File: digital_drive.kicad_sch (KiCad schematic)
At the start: 0 parts

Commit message: a bunch of updates
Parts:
- added U1601, U1602: EPC23104ENGRT, BR_Gate_Drivers:EPC23104, symbol BR_PMIC:EPC23104ENGRT

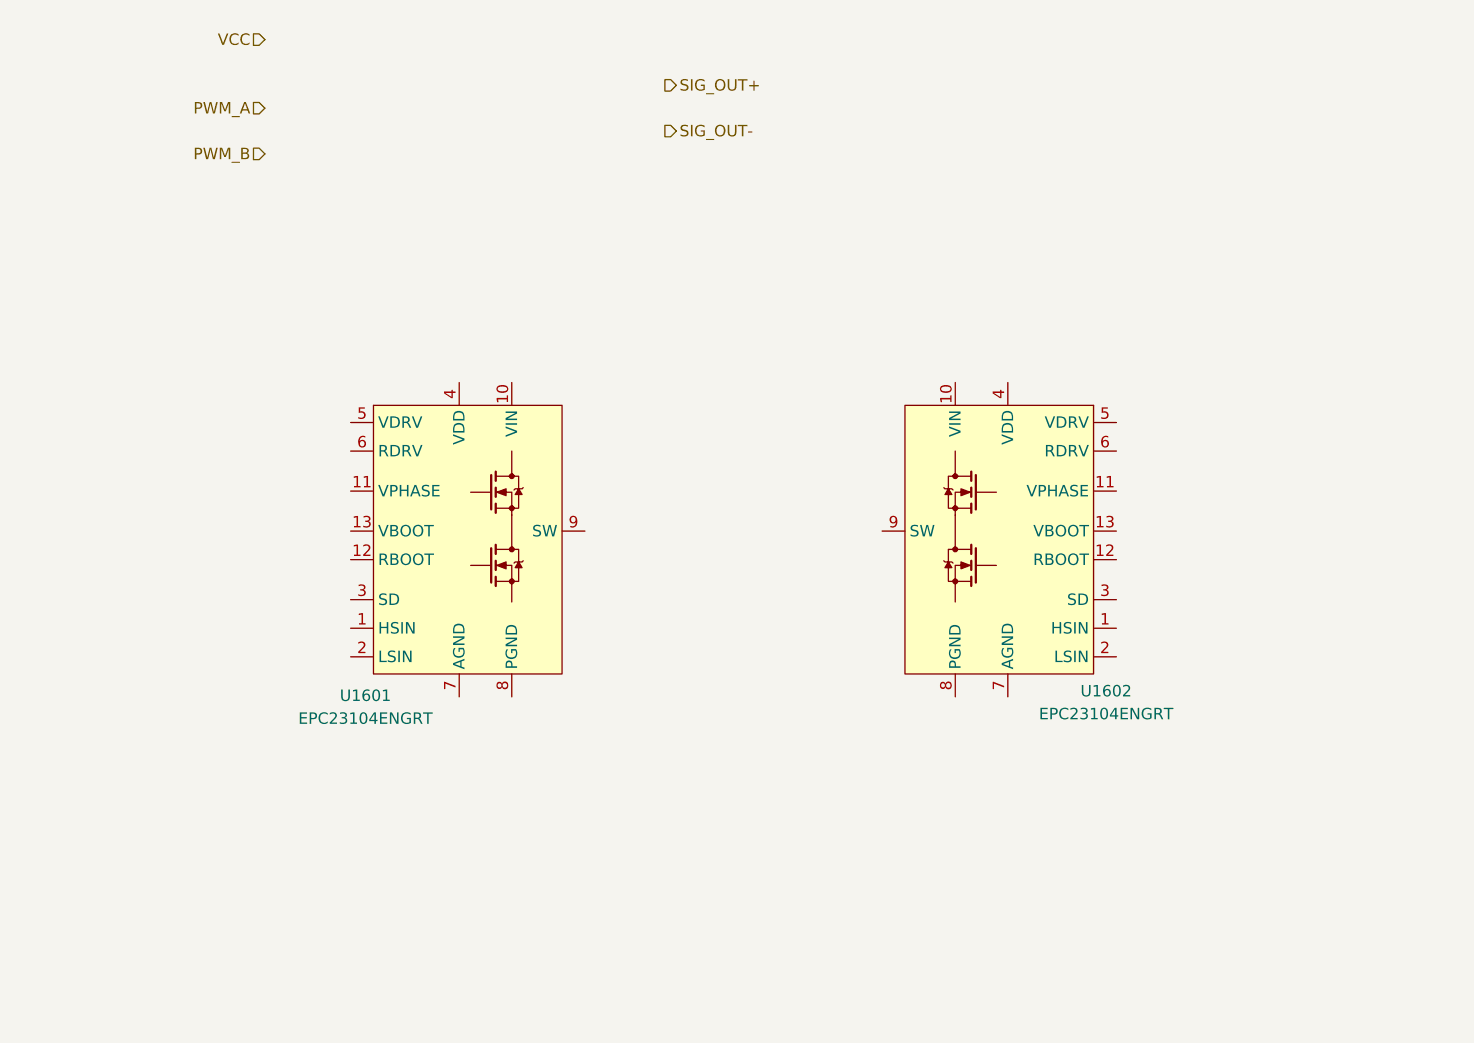
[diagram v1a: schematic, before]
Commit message: added rj45 and h-bridge + stm pinout spreadsheet
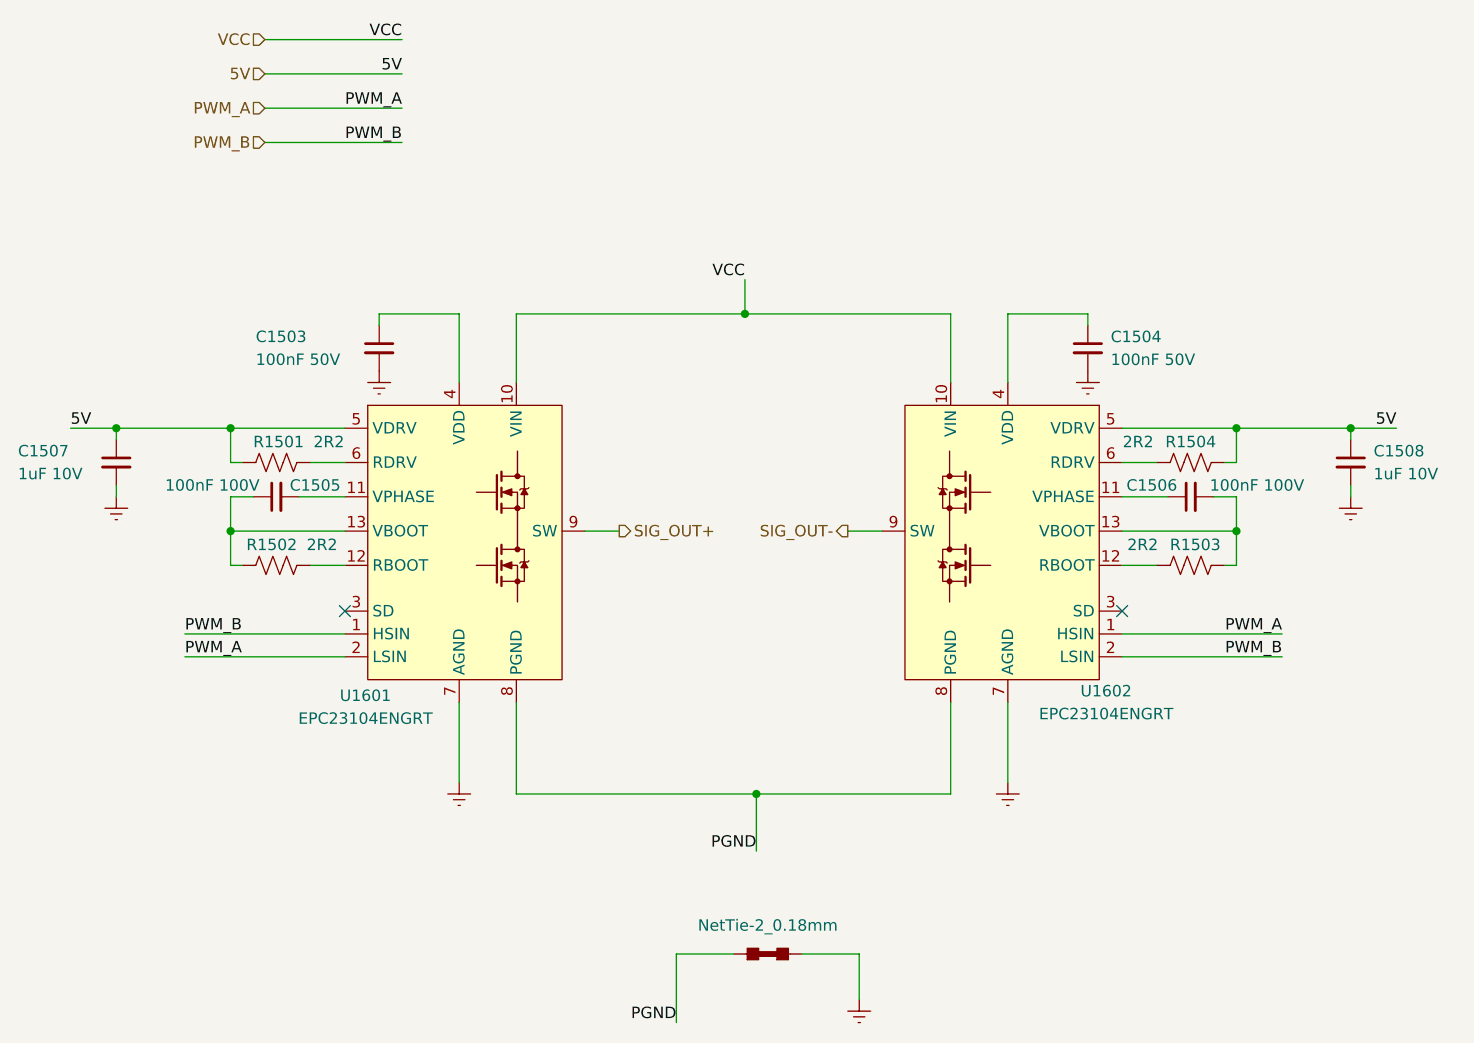
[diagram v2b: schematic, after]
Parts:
- added C1503, C1504: 100nF 50V, BR_Passives:C_0402_1005Metric-minimized, symbol BR_Capacitors_0402:C_0402_100nF_50V_X7R_10%_AEC-Q200
- added C1505, C1506: 100nF 100V, BR_Passives:C_0603_1608Metric-minimized, symbol BR_Capacitors_0603:C_0603_100nF_100V_X7R_AEC-Q200
- added C1507, C1508: 1uF 10V, BR_Passives:C_0402_1005Metric-minimized, symbol BR_Capacitors_0402:C_0402_1uF_10V_X7R_10%
- added NT1501: NetTie-2_0.18mm, BR_Virtual_Parts:NetTie-2_SMD_Pad_0.18mm_wide_long, symbol BR_Virtual_Parts:NetTie-2_0.18mm_long
- added R1501, R1502, R1503, R1504: 2R2, BR_Passives:R_0402_1005Metric-minimized, symbol BR_Resistors_0402:R_0402_2R2
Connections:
- net PWM_A: now also U1601.2 (LSIN), U1602.1 (HSIN)
- net PWM_B: now also U1601.1 (HSIN), U1602.2 (LSIN)
- net SIG_OUT+: now also U1601.9 (SW)
- net SIG_OUT-: now also U1602.9 (SW)
- net VCC: now also U1601.10 (VIN), U1602.10 (VIN)
- net at U1601.11 (VPHASE): now also C1505.2
- net at U1601.12 (RBOOT): now also R1502.2
- net at U1601.13 (VBOOT): now also C1505.1, R1502.1
- net at U1601.4 (VDD): now also C1503.1
- net 5V: now reaches U1601.5 (VDRV)
- net 5V: now also U1602.5 (VDRV), C1507.1, C1508.1, R1501.1, R1504.2
- net at U1601.6 (RDRV): now also R1501.2
- net GND: now reaches U1601.7 (AGND)
- net GND: now also U1602.7 (AGND), C1503.2, C1504.2, C1507.2, C1508.2, NT1501.2
- net PGND: now reaches U1601.8 (PGND)
- net PGND: now also U1602.8 (PGND), NT1501.1
- net at U1602.11 (VPHASE): now also C1506.1
- net at U1602.12 (RBOOT): now also R1503.1
- net at U1602.13 (VBOOT): now also C1506.2, R1503.2
- net at U1602.4 (VDD): now also C1504.1
- net at U1602.6 (RDRV): now also R1504.1
- no-connect marks 0 -> 2

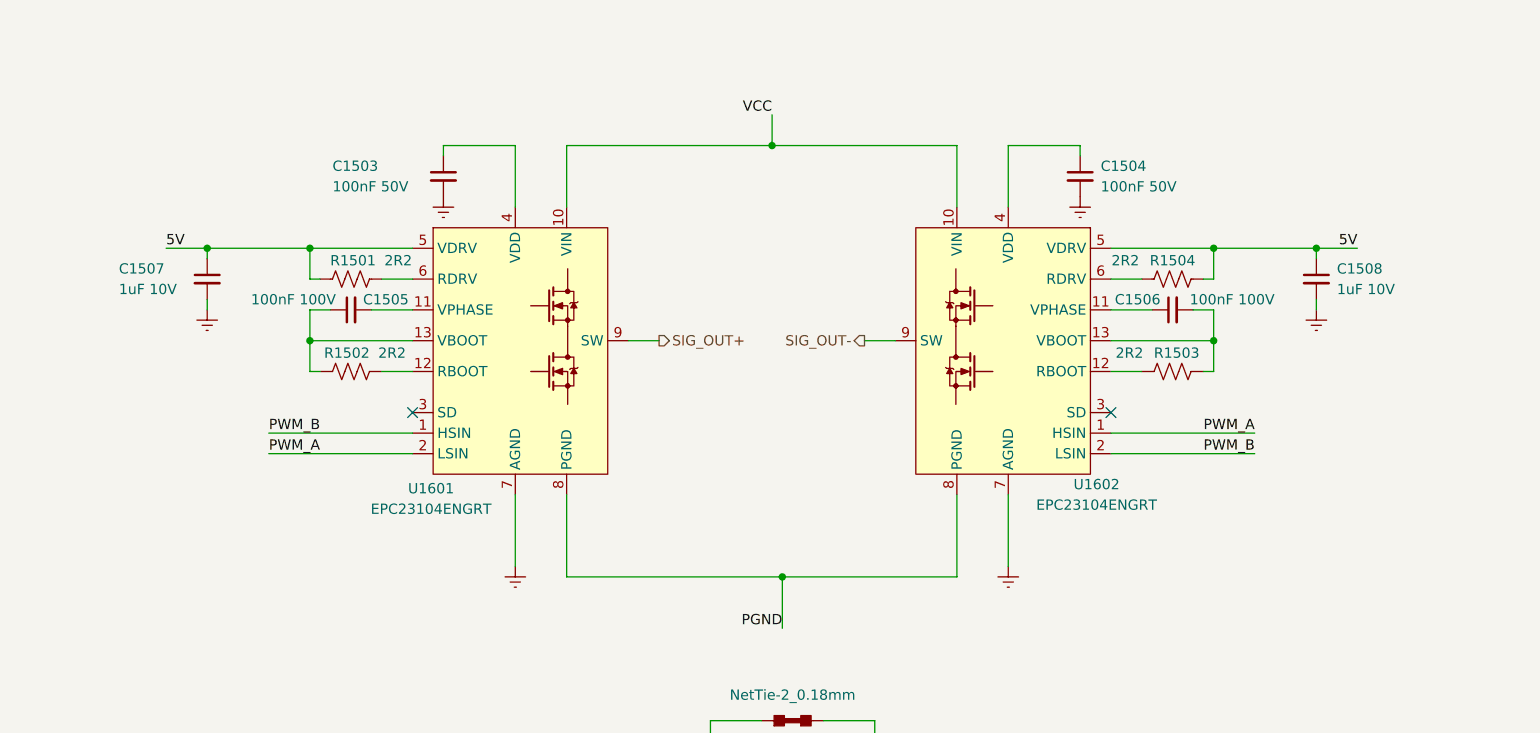
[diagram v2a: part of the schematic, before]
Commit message: implementing feedback + added stepper driver
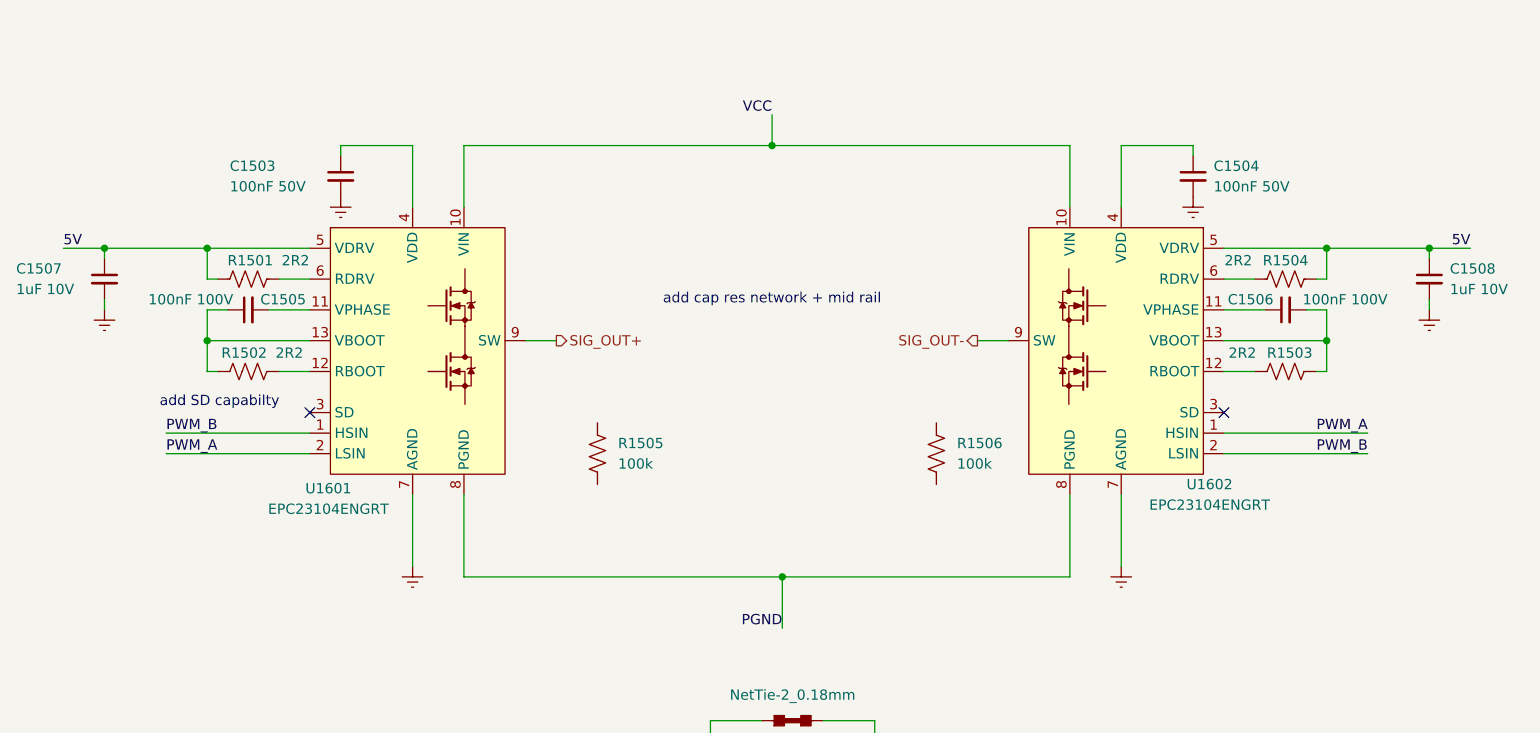
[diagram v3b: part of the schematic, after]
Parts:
- added R1505, R1506: 100k, BR_Passives:C_0402_1005Metric-minimized, symbol BR_Resistors_0402:R_0402_100k
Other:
- note added: "add SD capabilty"
- note added: "add cap res network + mid rail"
- moved on the sheet: C1503, C1504, C1505, C1506, C1507, C1508, R1501, R1502, R1503, R1504, U1601, U1602

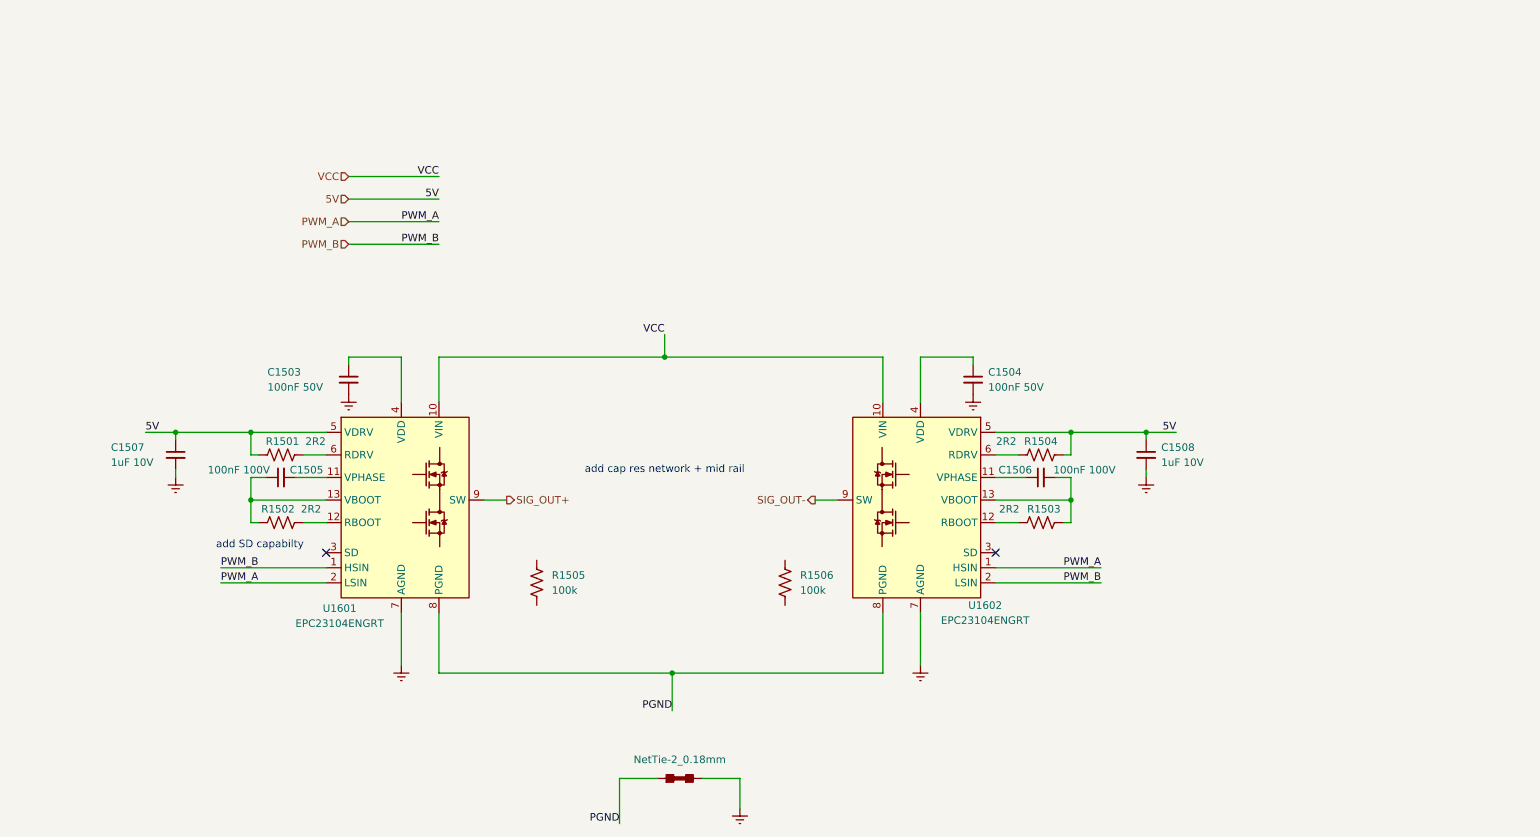
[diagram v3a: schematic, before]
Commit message: completed feedback from review + reannotated sheets
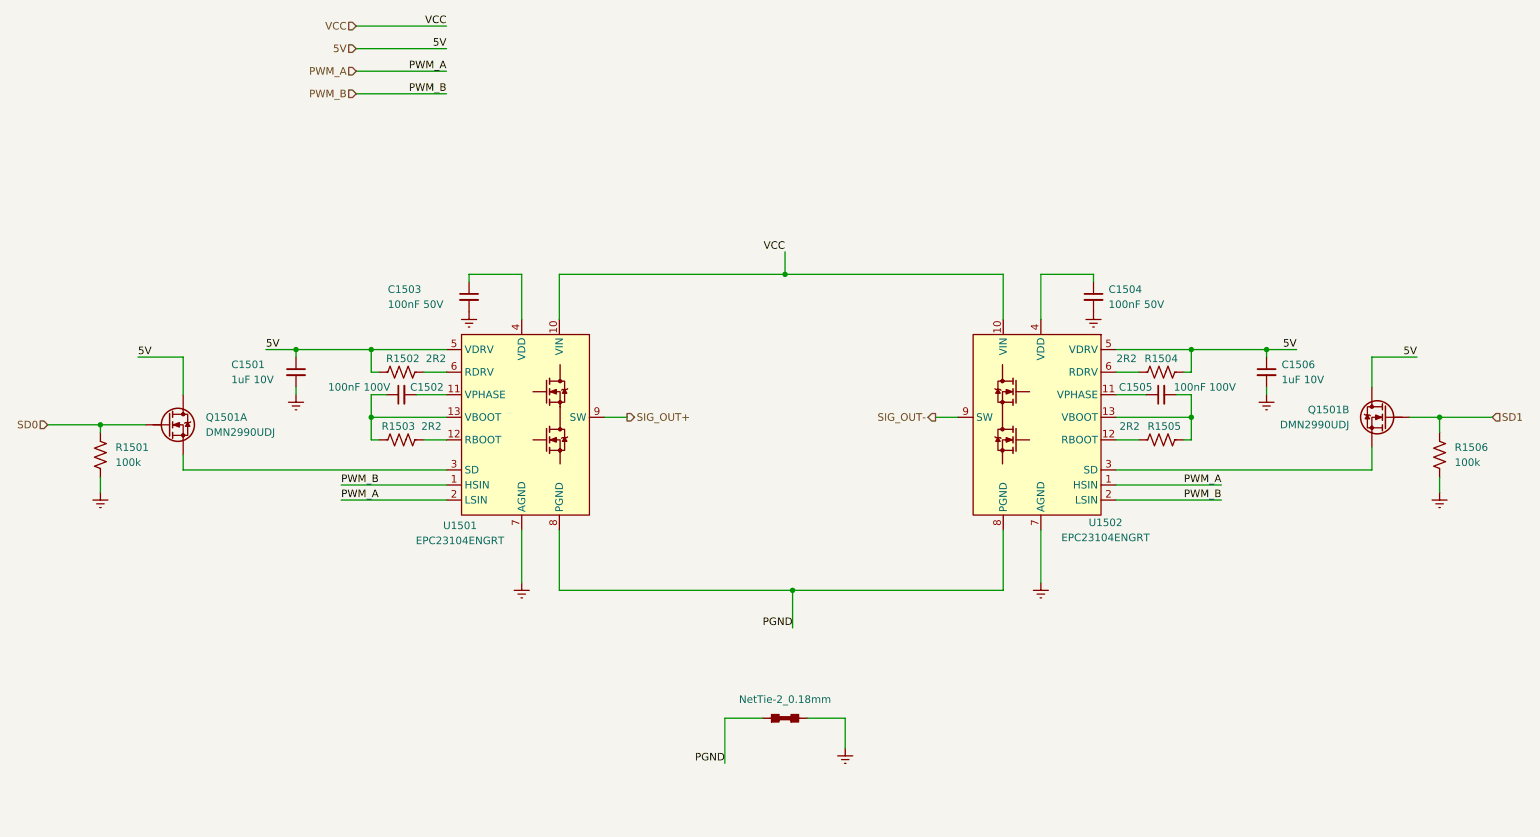
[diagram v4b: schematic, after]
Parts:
- removed R1505: 100k, BR_Passives:C_0402_1005Metric-minimized, symbol BR_Resistors_0402:R_0402_100k
- added Q1501: DMN2990UDJ, BR_SOT:SOT-963, symbol BR_Transistors:MFET_N_ARRAY_DMN2990UDJ-7
- added R1501: 100k, BR_Passives:C_0402_1005Metric-minimized, symbol BR_Resistors_0402:R_0402_100k
- renumbered C1507 to C1501, C1505 to C1502, C1506 to C1505, C1508 to C1506, R1501 to R1502, R1502 to R1503, R1503 to R1505, U1601 to U1501, U1602 to U1502
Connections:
- net 5V: now also Q1501.3, Q1501.6
- net GND: now also R1506.2, R1501.2
- net SD1: now reaches R1506.1
- net SD1: now also Q1501.5
- net at U1501.3 (SD): now also Q1501.1
- net at U1502.3 (SD): now also Q1501.4
- new net SD0: Q1501.2, R1501.1
- no-connect marks 2 -> 0
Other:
- note removed: "add SD capabilty"
- note removed: "add cap res network + mid rail"
- moved on the sheet: C1501, C1502, C1503, C1504, C1505, C1506, R1502, R1503, R1504, R1505, U1501, U1502

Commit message: modified SD feature
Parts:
- removed Q1501: DMN2990UDJ, BR_SOT:SOT-963, symbol BR_Transistors:MFET_N_ARRAY_DMN2990UDJ-7
- removed R1501, R1506: 100k, BR_Passives:C_0402_1005Metric-minimized, symbol BR_Resistors_0402:R_0402_100k
- added Q1501, Q1502, Q1503: MMBT3904L, BR_SOT:SOT-23, symbol BR_Transistors:BJT_N_MMBT3904L
- added R1501, R1508: 24k9, BR_Passives:C_0402_1005Metric-minimized, symbol BR_Resistors_0402:R_0402_24k9
- added R1506, R1507: 5k1, BR_Passives:C_0402_1005Metric-minimized, symbol BR_Resistors_0402:R_0402_5k1
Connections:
- net 5V: now also R1506.1, R1507.1
- net SD0: now also U1501.3 (SD), Q1501.2 (E)
- net SD1: now also U1502.3 (SD), Q1503.2 (E)
- new net: Q1501.3 (C), R1506.2
- new net: Q1503.3 (C), R1507.2
- new net: Q1501.1 (B), R1501.2
- new net: Q1503.1 (B), R1508.1
- new net 3V3: R1501.1, R1508.2
